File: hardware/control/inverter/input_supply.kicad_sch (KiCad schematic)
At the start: 17 parts, among them J1 RJ45, J2 RJ45, J3 RJ45, U1 L7812, U2 L7805, U3 74HC14, U4 74HC08, U5 74HC74

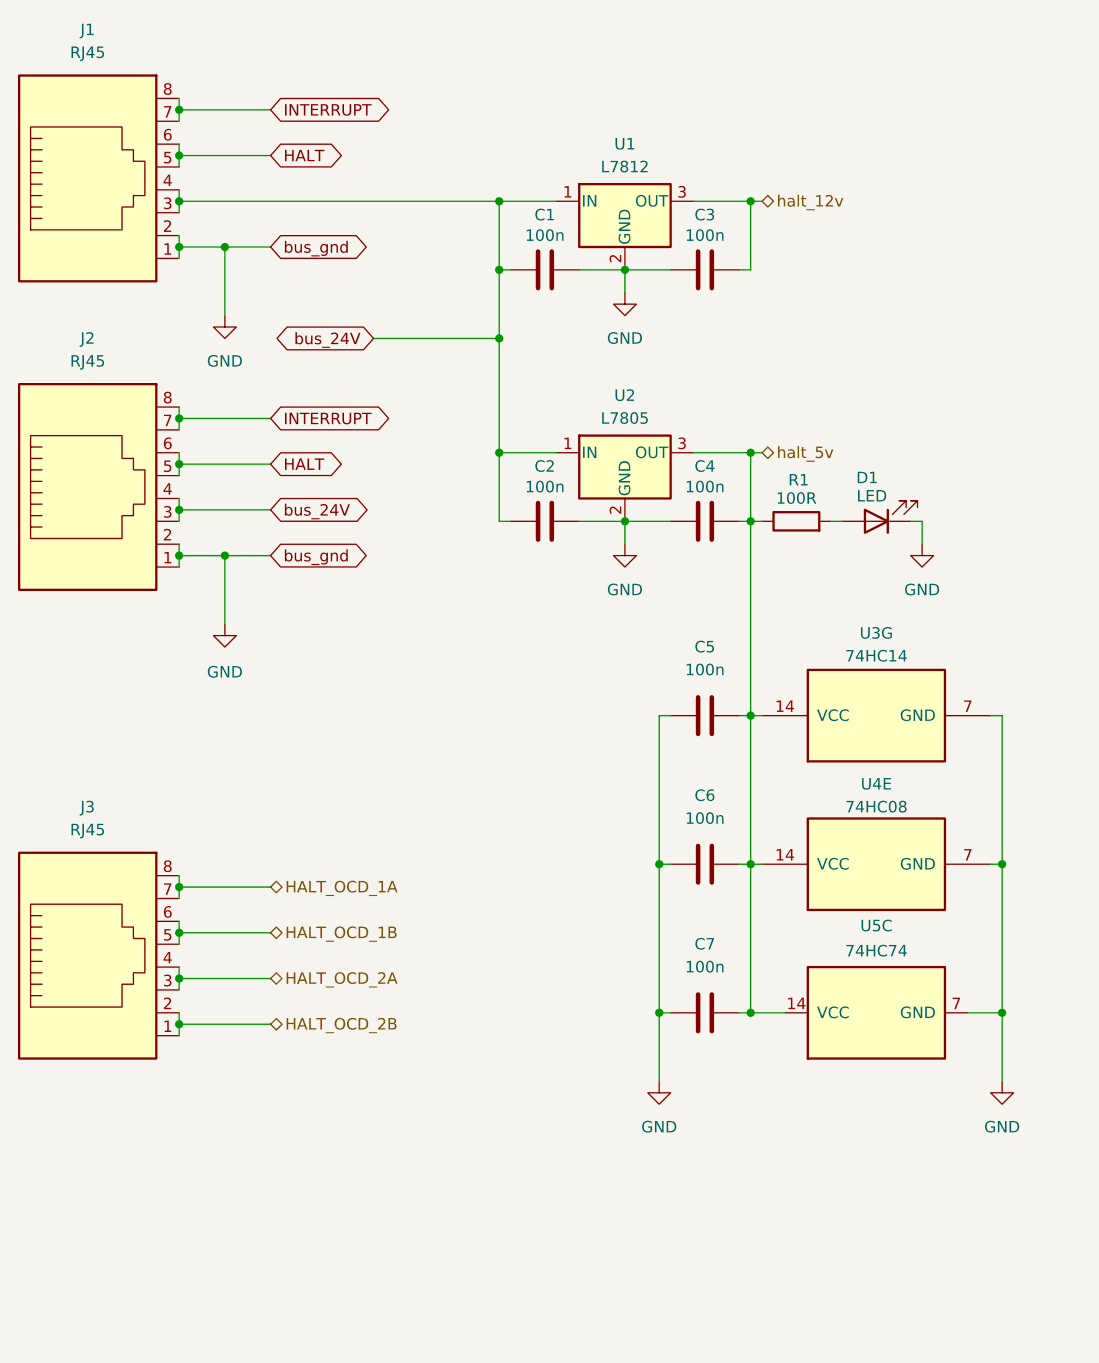
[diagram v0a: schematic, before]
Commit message: add progress on main drive controller and switch to hiearchical labels
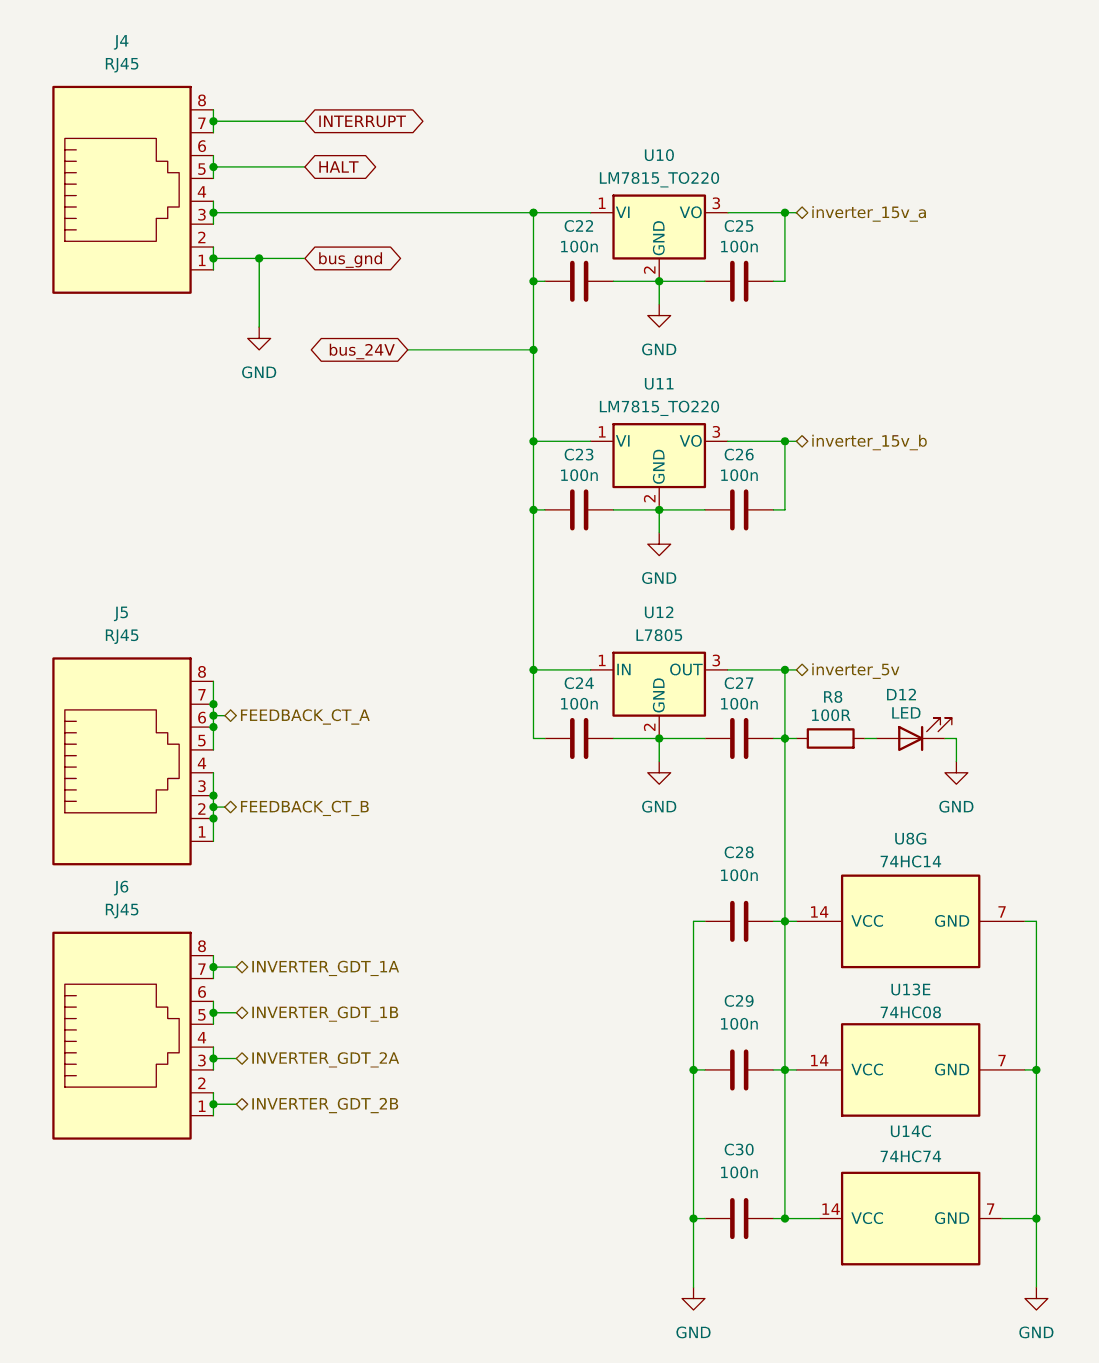
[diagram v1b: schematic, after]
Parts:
- removed C1, C2, C3, C4, C5, C6, C7: 100n, symbol Device:C
- removed D1: LED, symbol Device:LED
- removed J1, J2, J3: RJ45, symbol Connector:RJ45
- removed R1: 100R, symbol Device:R
- removed U1: L7812, symbol Regulator_Linear:L7812
- removed U2: L7805, symbol Regulator_Linear:L7805
- removed U3: 74HC14, symbol 74xx:74HC14
- removed U4: 74HC08, symbol 74xx:74HC00
- removed U5: 74HC74, symbol 74xx:74HC74
- added C22, C23, C24, C25, C26, C27, C28, C29, C30: 100n, symbol Device:C
- added D12: LED, symbol Device:LED
- added J4, J5, J6: RJ45, symbol Connector:RJ45
- added R8: 100R, symbol Device:R
- added U10, U11: LM7815_TO220, Package_TO_SOT_THT:TO-220-3_Vertical, symbol Regulator_Linear:LM7815_TO220
- added U12: L7805, symbol Regulator_Linear:L7805
- added U13: 74HC08, symbol 74xx:74HC00
- added U14: 74HC74, symbol 74xx:74HC74
- added U8: 74HC14, symbol 74xx:74HC14
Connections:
- net GND: now also C22.2, C23.2, C24.2, C25.1, C26.1, C27.1, C28.1, C29.1, C30.1, D12.1 (K), J4.1, J4.2, U10.2 (GND), U11.2 (GND), U12.2 (GND), U13.7 (GND), U14.7 (GND), U8.7 (GND)
- net HALT: now also J4.5, J4.6
- net INTERRUPT: now also J4.7, J4.8
- net bus_24V: now also C22.1, C23.1, C24.1, J4.3, J4.4, U10.1 (VI), U11.1 (VI), U12.1 (IN)
- new net: D12.2 (A), R8.2
- new net FEEDBACK_CT_A: J5.5, J5.6, J5.7, J5.8
- new net FEEDBACK_CT_B: J5.1, J5.2, J5.3, J5.4
- new net INVERTER_GDT_1A: J6.7, J6.8
- new net INVERTER_GDT_1B: J6.5, J6.6
- new net INVERTER_GDT_2A: J6.3, J6.4
- new net INVERTER_GDT_2B: J6.1, J6.2
- new net inverter_15v_a: C25.2, U10.3 (VO)
- new net inverter_15v_b: C26.2, U11.3 (VO)
- new net inverter_5v: C27.2, C28.2, C29.2, C30.2, R8.1, U12.3 (OUT), U13.14 (VCC), U14.14 (VCC), U8.14 (VCC)
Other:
- company: Author: 9551 (devvie.cc) -> (none)
- title: QCW DRSSTC halt board input stage -> (none)

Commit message: update right about freaking everything
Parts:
- removed U13: 74HC08, symbol 74xx:74HC00
- added U20: 74LS08, symbol 74xx:74LS08
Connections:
- net GND: now also U20.7 (GND)
- net inverter_5v: now also U20.14 (VCC)

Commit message: idk some changes
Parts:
- removed C22, C23, C25, C26: 100n, symbol Device:C
- removed U10, U11: LM7815_TO220, Package_TO_SOT_THT:TO-220-3_Vertical, symbol Regulator_Linear:LM7815_TO220
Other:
- moved on the sheet: C24, C27, C28, C29, C30, D12, R8, U12, U14C, U20E, U8G

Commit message: completed-ish inverter board, probably not, but anyway
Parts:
- added C23, C25: 100n, symbol Device:C
- added U17: L7812, symbol Regulator_Linear:L7812
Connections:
- net GND: now also C23.2, C25.1, U17.2 (GND)
- net bus_24V: now also C23.1, U17.1 (IN)
- new net inverter_12v: C25.2, U17.3 (OUT)
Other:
- moved on the sheet: C24, C27, C28, C29, C30, D12, R8, U12, U14C, U20E, U8G

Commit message: minor changes
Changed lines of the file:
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@@
-	)
-	(junction
-		(at 78.74 60.96)
-		(diameter 0)
-		(color 0 0 0 0)
 	)
 	(junction
@@
 	(wire
 		(pts
+			(xy 78.74 53.34) (xy 78.74 77.47)
+		)
+		(stroke
+			(width 0)
+			(type default)
+		)
+	)
+	(wire
+		(pts
 			(xy 135.89 138.43) (xy 132.08 138.43)
 		)
@@
 	(wire
 		(pts
-			(xy 78.74 53.34) (xy 78.74 60.96)
-		)
-		(stroke
-			(width 0)
-			(type default)
-		)
-	)
-	(wire
-		(pts
-			(xy 78.74 60.96) (xy 63.5 60.96)
+			(xy 78.74 53.34) (xy 76.2 53.34)
 		)
 		(stroke
@@
 		(pts
 			(xy 41.91 44.45) (xy 41.91 45.72)
-		)
-		(stroke
-			(width 0)
-			(type default)
-		)
-	)
-	(wire
-		(pts
-			(xy 78.74 77.47) (xy 78.74 60.96)
 		)
 		(stroke
@@
 	(global_label "bus_24V"
 		(shape bidirectional)
-		(at 63.5 60.96 180)
+		(at 76.2 53.34 180)
 		(fields_autoplaced yes)
 		(effects
@@
 		)
 		(property "Intersheetrefs" "${INTERSHEET_REFS}"
-			(at 51.6022 60.96 0)
+			(at 64.3022 53.34 0)
 			(effects
 				(font
